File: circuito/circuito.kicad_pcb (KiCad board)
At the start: 2 copper layers, 6 parts, among them J1 Alimentação, Q1 BC558, U1 Pico

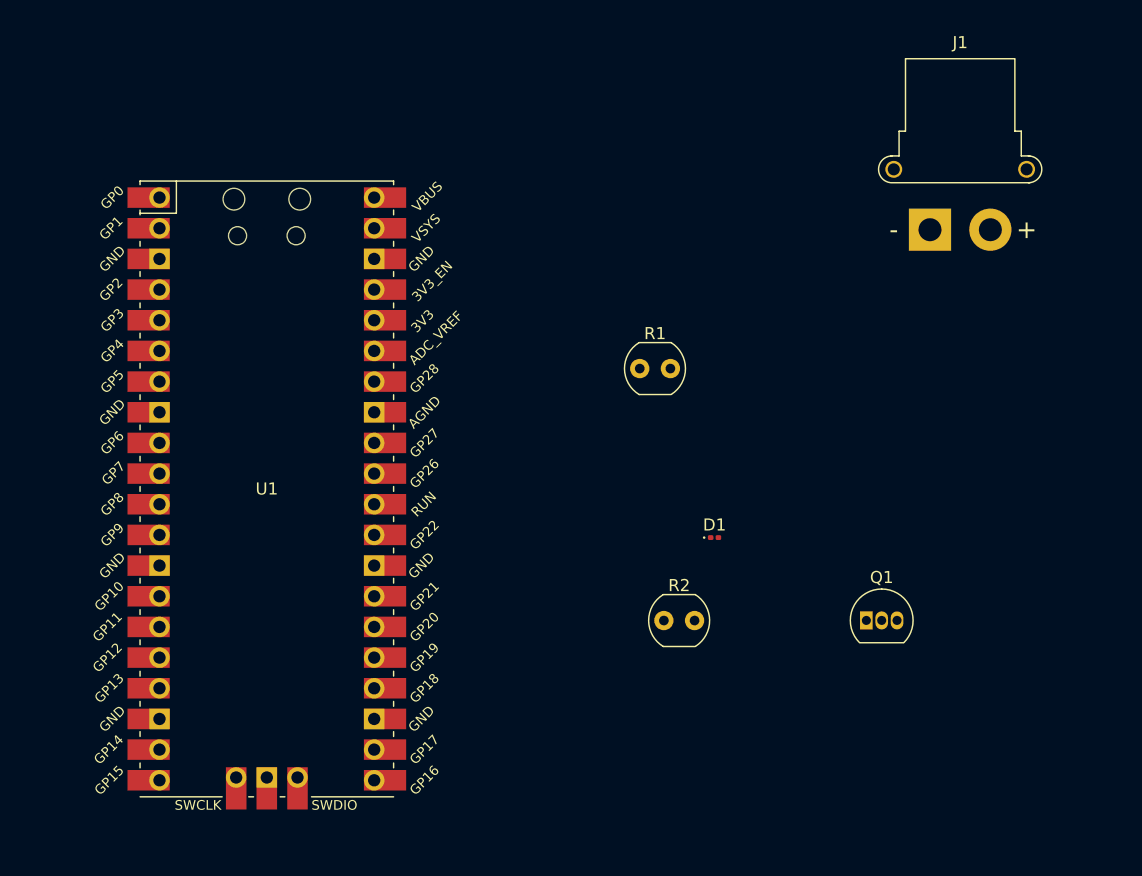
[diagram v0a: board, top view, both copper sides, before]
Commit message: feat introdução das linhas na pcb e visualizador 3D
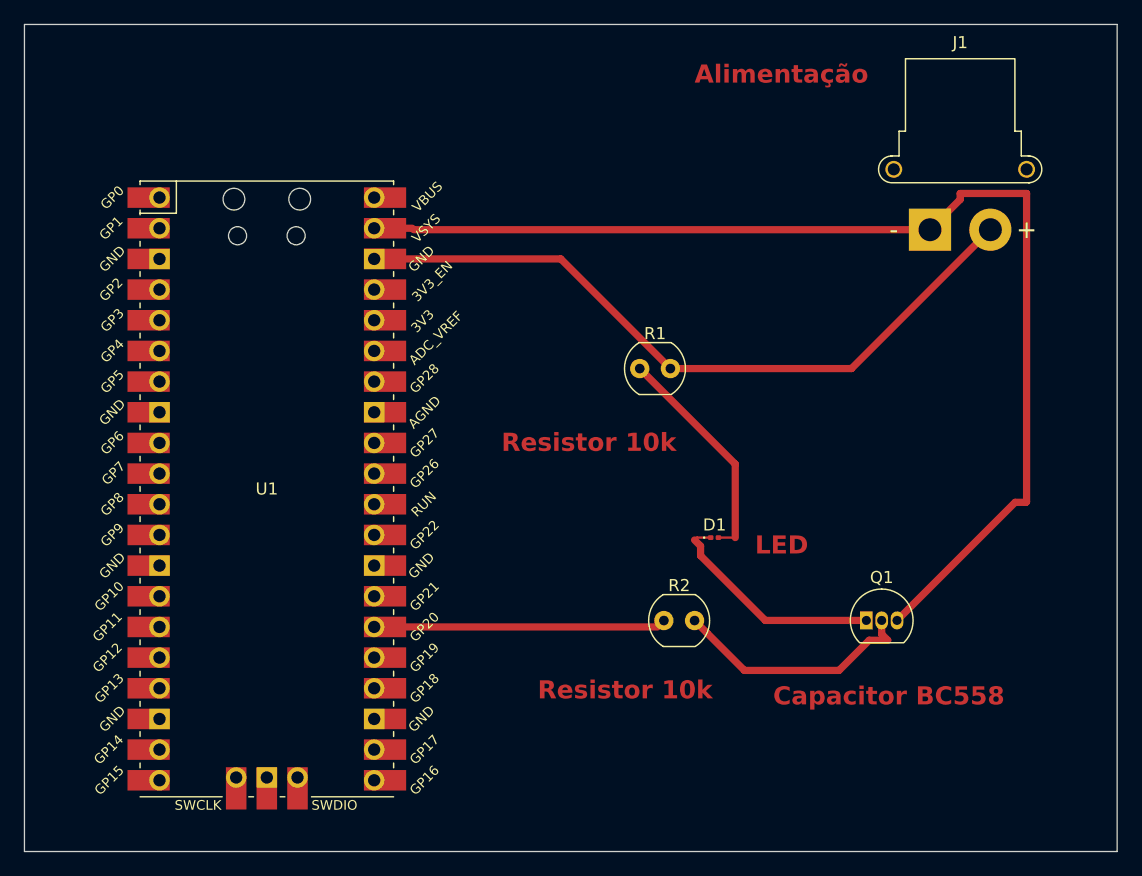
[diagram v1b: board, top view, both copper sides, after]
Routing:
- net VCC: track 0.00 -> 96.0 mm
- net GND: track 0.00 -> 59.6 mm
- net Net-(U1-GPIO20): track 0.00 -> 24.2 mm
- net Net-(Q1-B): track 0.00 -> 20.6 mm
- net Net-(D1-K): track 0.00 -> 18.9 mm
- net Net-(D1-A): track 0.00 -> 18.7 mm
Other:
- board outline added: 90.5 x 68.5 mm
- board text added: "Alimentação"
- board text added: "Capacitor BC558"
- board text added: "LED"
- board text added: "PCB - José V. Alencar"
- board text added: "Resistor 10k"
